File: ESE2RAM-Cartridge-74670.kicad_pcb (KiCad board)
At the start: 2 copper layers, 100 x 60.5 mm, 26 parts, among them IC1 SRAM, IC2 SRAM, J1 BUS_MSX, U1 74HC670, U2 74HC670, U3 74HC138, U4 74HC00, U5 74HC32

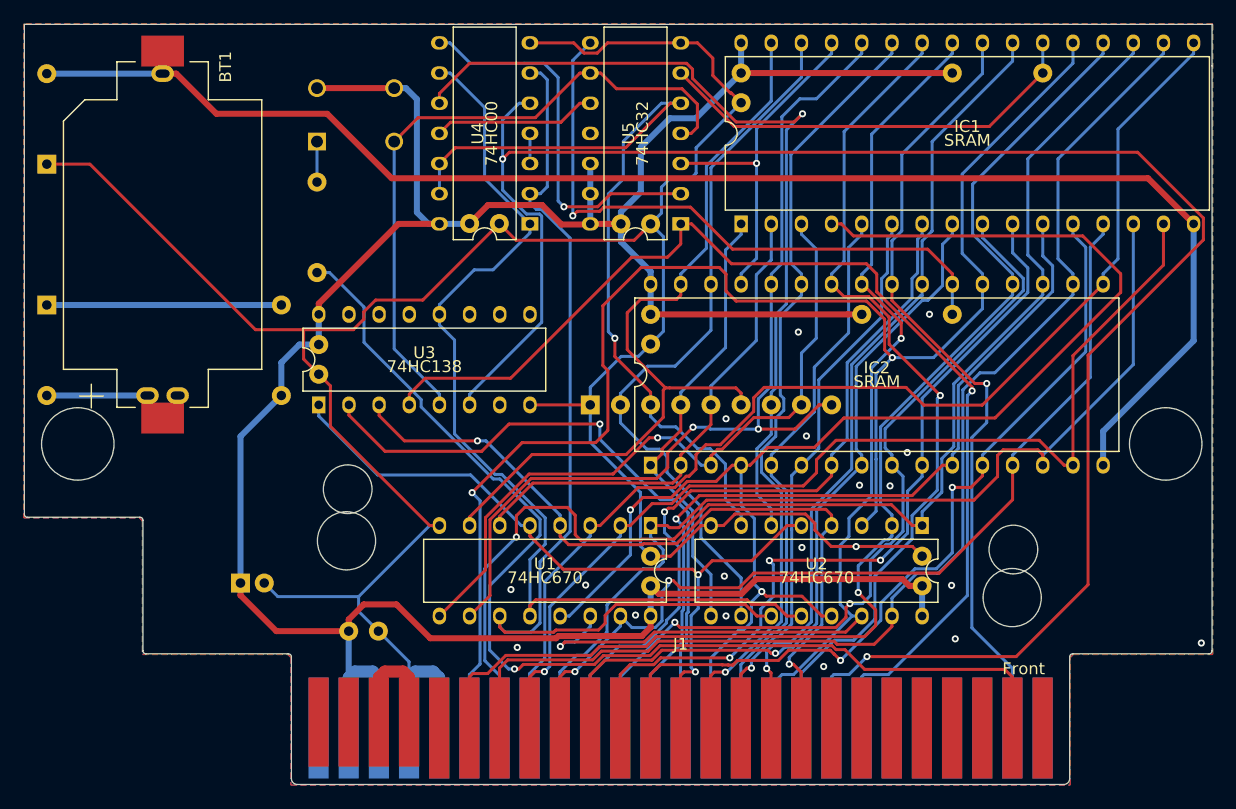
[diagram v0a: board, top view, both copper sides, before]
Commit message: Modify Schematic
プロジェクトローカルライブラリの設定が抜けていたのを修正。
Fixed missing project local library settings.
その他の細かな修正。
Other minor corrections.
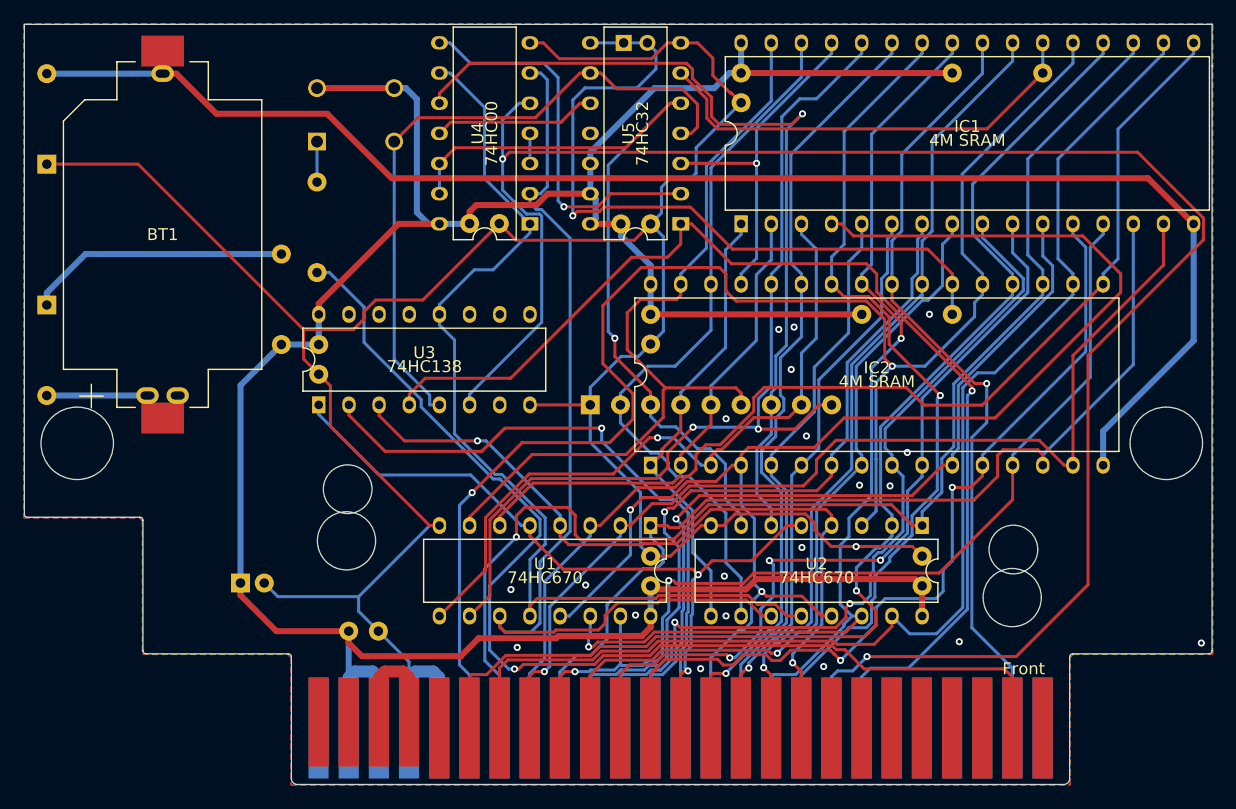
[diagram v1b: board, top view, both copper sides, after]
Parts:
- added J2: 8M, Connector_PinHeader_2.00mm:PinHeader_1x02_P2.00mm_Vertical, B.Cu at (90.2, 100.9)
- BT1: footprint _GoriponsoftLibrary:BatteryHolder_CH2x-2032LF -> ProjectLibrary:BatteryHolder_CH2x-2032LF
- IC1, IC2: value SRAM -> 4M SRAM; footprint _GoriponsoftLibrary:DIP32_600mil_FineLongPad -> ProjectLibrary:DIP32_600mil_FineLongPad
- S1: footprint SamacSys_Parts:DTS63NV -> ProjectLibrary:DTS63NV
- U1, U2, U3: footprint _GoriponsoftLibrary:DIP16_300mil_FineLongPad -> ProjectLibrary:DIP16_300mil_FineLongPad
- U4, U5: footprint _GoriponsoftLibrary:DIP14_300mil_FineLongPad -> ProjectLibrary:DIP14_300mil_FineLongPad
- moved R4 4.29 mm to (61.4, 126.3)
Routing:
- net /~{RAM1_CE}: track 53.2 -> 63.1 mm
- net /D0: track 78.4 -> 82.7 mm
- net /D4: track 101.2 -> 104.6 mm
- net /A11: track 99.6 -> 96.3 mm
- net /D7: track 127.4 -> 130.3 mm
- net Net-(D2-K): track 19.8 -> 22.1 mm
- net /A0: track 69.5 -> 71.7 mm
- net /A3: track 68.6 -> 70.2 mm
- net /A5: track 62.7 -> 64.3 mm
- net +5V: track 237.2 -> 235.7 mm
- net /EN_WR: track 72.0 -> 73.1 mm
- net /~{RAM0_CE}: track 36.7 -> 37.9 mm
- net /~{WR}: track 95.6 -> 96.2 mm
- net /A13: track 63.7 -> 63.2 mm
- net /A12: track 119.9 -> 120.5 mm
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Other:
- board text added: "似非²RAM rev.3 Goripon Hardware"
- board text removed: "似非²RAM rev.2 Goripon Hardware"

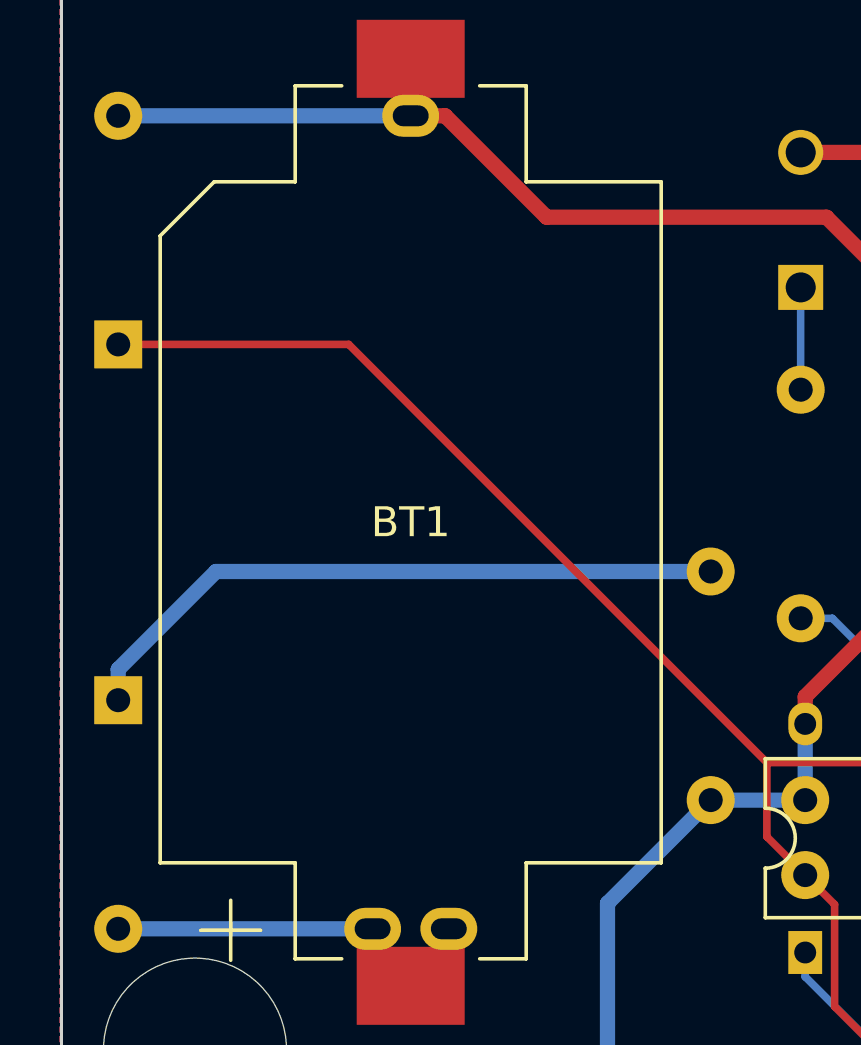
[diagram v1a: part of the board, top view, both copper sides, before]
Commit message: Modified Schematic
電解コンデンサの容量を10μFから47μFに変更
電池ソケットのシルク印刷の切り欠き位置が間違っていたのを修正
不要なファイルの削除
その他細かな修正
Changed the capacitance of electrolytic capacitor from 10uF to 47uF.
Fixed an issue where the notch position on the silkscreen print on the battery socket was incorrect.
Delete unnecessary files.
Other minor corrections.
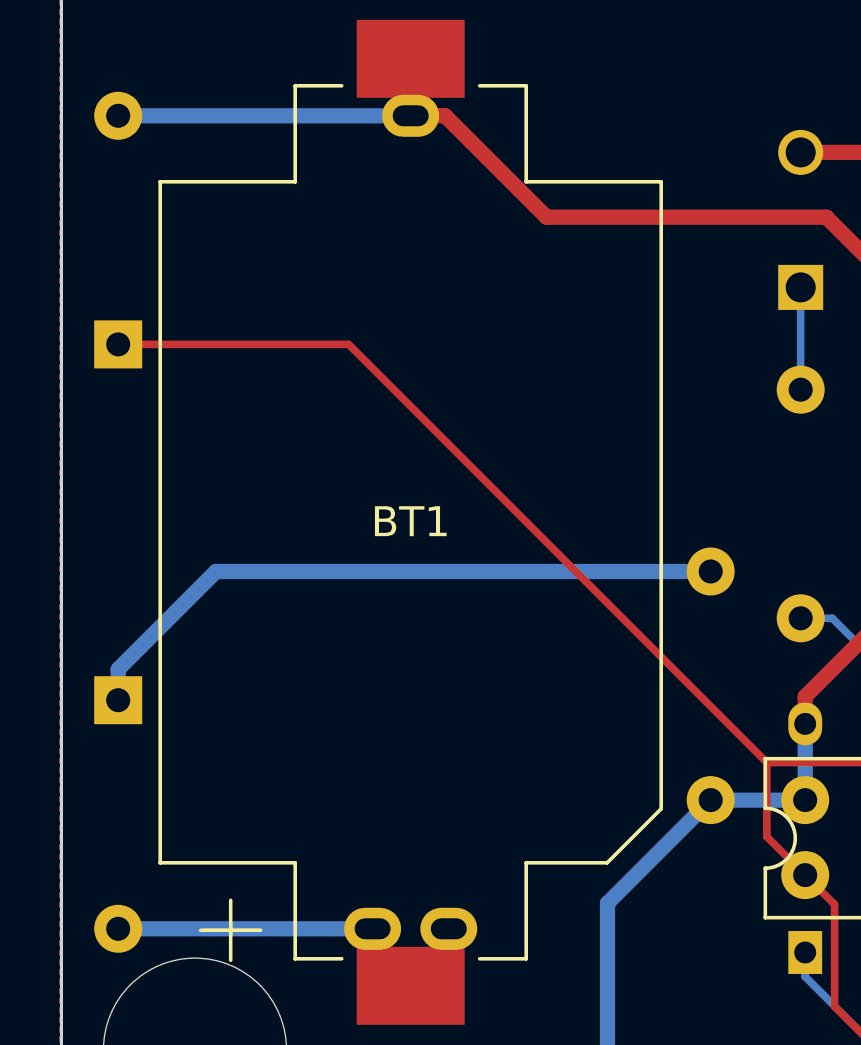
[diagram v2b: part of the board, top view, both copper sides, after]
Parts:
- C9: value 10u -> 47u
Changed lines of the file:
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@@
       (net 22 "/D6") (pinfunction "D6") (pintype "passive"))
     (pad "41" connect rect (at -20.32 -0.44) (size 1.7 8.5) (layers "B.Cu" "B.Mask")
-      (net 2 "GND") (pinfunction "GND") (pintype "passive"))
+      (net 2 "GND") (pinfunction "GND") (pintype "passive") (zone_connect 2))
     (pad "42" connect rect (at -20.32 -0.44) (size 1.7 8.5) (layers "F.Cu" "F.Mask")
       (net 51 "unconnected-(J1-CLOCK-Pad42)") (pinfunction "CLOCK") (pintype "passive+no_connect"))
     (pad "43" connect rect (at -22.86 -0.44) (size 1.7 8.5) (layers "B.Cu" "B.Mask")
-      (net 2 "GND") (pinfunction "GND") (pintype "passive"))
+      (net 2 "GND") (pinfunction "GND") (pintype "passive") (zone_connect 2))
     (pad "44" connect rect (at -22.86 -0.94) (size 1.7 7.5) (layers "F.Cu" "F.Mask")
       (net 52 "Net-(J1-SW1)") (pinfunction "SW1") (pintype "passive"))
@@
     (fp_line (start -11.35 -8.35) (end -11.35 -3.85)
       (stroke (width 0.12) (type solid)) (layer "F.SilkS"))
-    (fp_line (start -11.35 -8.35) (end 11.35 -8.35)
+    (fp_line (start -11.35 -8.35) (end 9.55 -8.35)
       (stroke (width 0.12) (type solid)) (layer "F.SilkS"))
     (fp_line (start -11.35 -3.85) (end -14.55 -3.85)
@@
     (fp_line (start -11.35 3.85) (end -14.55 3.85)
       (stroke (width 0.12) (type solid)) (layer "F.SilkS"))
-    (fp_line (start -11.35 6.55) (end -11.35 3.85)
-      (stroke (width 0.12) (type solid)) (layer "F.SilkS"))
-    (fp_line (start -9.55 8.35) (end -11.35 6.55)
-      (stroke (width 0.12) (type solid)) (layer "F.SilkS"))
-    (fp_line (start 11.35 -8.35) (end 11.35 -3.85)
+    (fp_line (start -11.35 8.35) (end -11.35 3.85)
+      (stroke (width 0.12) (type solid)) (layer "F.SilkS"))
+    (fp_line (start 9.55 -8.35) (end 11.35 -6.55)
+      (stroke (width 0.12) (type solid)) (layer "F.SilkS"))
+    (fp_line (start 11.35 -6.55) (end 11.35 -3.85)
       (stroke (width 0.12) (type solid)) (layer "F.SilkS"))
     (fp_line (start 11.35 -3.85) (end 14.55 -3.85)
@@
     (fp_line (start 11.35 3.85) (end 14.55 3.85)
       (stroke (width 0.12) (type solid)) (layer "F.SilkS"))
-    (fp_line (start 11.35 8.35) (end -9.55 8.35)
+    (fp_line (start 11.35 8.35) (end -11.35 8.35)
       (stroke (width 0.12) (type solid)) (layer "F.SilkS"))
     (fp_line (start 11.35 8.35) (end 11.35 3.85)
@@
     (fp_circle (center 0 0) (end -10.2 0)
       (stroke (width 0.3) (type solid)) (fill none) (layer "Dwgs.User"))
-    (fp_line (start -17.2 2.3) (end -17.2 -2.3)
-      (stroke (width 0.05) (type solid)) (layer "F.CrtYd"))
-    (fp_line (start -17.2 2.3) (end -14.7 2.3)
-      (stroke (width 0.05) (type default)) (layer "F.CrtYd"))
+    (fp_line (start -17.2 -2.3) (end -17.2 2.3)
+      (stroke (width 0.05) (type solid)) (layer "F.CrtYd"))
+    (fp_line (start -14.7 -4) (end -14.7 -2.3)
+      (stroke (width 0.05) (type solid)) (layer "F.CrtYd"))
     (fp_line (start -14.7 -4) (end -11.5 -4)
       (stroke (width 0.05) (type solid)) (layer "F.CrtYd"))
     (fp_line (start -14.7 -2.3) (end -17.2 -2.3)
       (stroke (width 0.05) (type default)) (layer "F.CrtYd"))
-    (fp_line (start -14.7 -2.3) (end -14.7 -4)
-      (stroke (width 0.05) (type solid)) (layer "F.CrtYd"))
-    (fp_line (start -14.7 4) (end -14.7 2.3)
-      (stroke (width 0.05) (type solid)) (layer "F.CrtYd"))
-    (fp_line (start -14.7 4) (end -11.5 4)
+    (fp_line (start -14.7 2.3) (end -17.2 2.3)
+      (stroke (width 0.05) (type default)) (layer "F.CrtYd"))
+    (fp_line (start -14.7 2.3) (end -14.7 4)
       (stroke (width 0.05) (type solid)) (layer "F.CrtYd"))
     (fp_line (start -11.5 -8.5) (end -6.5 -8.5)
@@
     (fp_line (start -11.5 -4) (end -11.5 -8.5)
       (stroke (width 0.05) (type solid)) (layer "F.CrtYd"))
-    (fp_line (start -11.5 4) (end -11.5 8.5)
-      (stroke (width 0.05) (type solid)) (layer "F.CrtYd"))
-    (fp_line (start -6.5 8.5) (end -11.5 8.5)
-      (stroke (width 0.05) (type solid)) (layer "F.CrtYd"))
-    (fp_line (start 11.5 -8.5) (end 6.5 -8.5)
-      (stroke (width 0.05) (type solid)) (layer "F.CrtYd"))
-    (fp_line (start 11.5 -8.5) (end 11.5 -4)
-      (stroke (width 0.05) (type solid)) (layer "F.CrtYd"))
-    (fp_line (start 11.5 -4) (end 14.7 -4)
+    (fp_line (start -11.5 4) (end -14.7 4)
+      (stroke (width 0.05) (type solid)) (layer "F.CrtYd"))
+    (fp_line (start -11.5 8.5) (end -11.5 4)
+      (stroke (width 0.05) (type solid)) (layer "F.CrtYd"))
+    (fp_line (start -11.5 8.5) (end -6.5 8.5)
+      (stroke (width 0.05) (type solid)) (layer "F.CrtYd"))
+    (fp_line (start 6.5 -8.5) (end 11.5 -8.5)
+      (stroke (width 0.05) (type solid)) (layer "F.CrtYd"))
+    (fp_line (start 11.5 -4) (end 11.5 -8.5)
       (stroke (width 0.05) (type solid)) (layer "F.CrtYd"))
     (fp_line (start 11.5 4) (end 11.5 8.5)
@@
     (fp_line (start 11.5 8.5) (end 6.5 8.5)
       (stroke (width 0.05) (type solid)) (layer "F.CrtYd"))
-    (fp_line (start 14.7 -2.3) (end 14.7 -4)
-      (stroke (width 0.05) (type solid)) (layer "F.CrtYd"))
-    (fp_line (start 14.7 -2.3) (end 17.2 -2.3)
-      (stroke (width 0.05) (type default)) (layer "F.CrtYd"))
+    (fp_line (start 14.7 -4) (end 11.5 -4)
+      (stroke (width 0.05) (type solid)) (layer "F.CrtYd"))
+    (fp_line (start 14.7 -4) (end 14.7 -2.3)
+      (stroke (width 0.05) (type solid)) (layer "F.CrtYd"))
+    (fp_line (start 14.7 2.3) (end 14.7 4)
+      (stroke (width 0.05) (type solid)) (layer "F.CrtYd"))
     (fp_line (start 14.7 2.3) (end 17.2 2.3)
       (stroke (width 0.05) (type default)) (layer "F.CrtYd"))
     (fp_line (start 14.7 4) (end 11.5 4)
       (stroke (width 0.05) (type solid)) (layer "F.CrtYd"))
-    (fp_line (start 14.7 4) (end 14.7 2.3)
-      (stroke (width 0.05) (type solid)) (layer "F.CrtYd"))
-    (fp_line (start 17.2 2.3) (end 17.2 -2.3)
+    (fp_line (start 17.2 -2.3) (end 14.7 -2.3)
+      (stroke (width 0.05) (type default)) (layer "F.CrtYd"))
+    (fp_line (start 17.2 -2.3) (end 17.2 2.3)
       (stroke (width 0.05) (type solid)) (layer "F.CrtYd"))
     (fp_arc (start -6.499999 -8.5) (mid 0 -10.700467) (end 6.5 -8.5)
       (stroke (width 0.05) (type solid)) (layer "F.CrtYd"))
-    (fp_arc (start 6.499999 8.5) (mid 0 10.700467) (end -6.5 8.5)
-      (stroke (width 0.05) (type solid)) (layer "F.CrtYd"))
-    (fp_line (start -14.2 -3.5) (end -11 -3.5)
-      (stroke (width 0.1) (type solid)) (layer "F.Fab"))
-    (fp_line (start -14.2 3.5) (end -14.2 -3.5)
+    (fp_arc (start 6.5 8.5) (mid 0 10.700467) (end -6.499999 8.5)
+      (stroke (width 0.05) (type solid)) (layer "F.CrtYd"))
+    (fp_line (start -14.2 3.5) (end -11 3.5)
       (stroke (width 0.1) (type solid)) (layer "F.Fab"))
     (fp_line (start -11 -8) (end -11 -3.5)
       (stroke (width 0.1) (type solid)) (layer "F.Fab"))
-    (fp_line (start -11 3.5) (end -14.2 3.5)
-      (stroke (width 0.1) (type solid)) (layer "F.Fab"))
-    (fp_line (start -11 6.4) (end -11 3.5)
-      (stroke (width 0.1) (type solid)) (layer "F.Fab"))
-    (fp_line (start -9.4 8) (end -11 6.4)
-      (stroke (width 0.1) (type solid)) (layer "F.Fab"))
-    (fp_line (start 11 -8) (end -11 -8)
-      (stroke (width 0.1) (type solid)) (layer "F.Fab"))
-    (fp_line (start 11 -8) (end 11 -3.5)
-      (stroke (width 0.1) (type solid)) (layer "F.Fab"))
-    (fp_line (start 11 3.5) (end 14.2 3.5)
-      (stroke (width 0.1) (type solid)) (layer "F.Fab"))
-    (fp_line (start 11 8) (end -9.4 8)
+    (fp_line (start -11 -8) (end 9.4 -8)
+      (stroke (width 0.1) (type solid)) (layer "F.Fab"))
+    (fp_line (start -11 -3.5) (end -14.2 -3.5)
+      (stroke (width 0.1) (type solid)) (layer "F.Fab"))
+    (fp_line (start -11 8) (end -11 3.5)
+      (stroke (width 0.1) (type solid)) (layer "F.Fab"))
+    (fp_line (start -11 8) (end 11 8)
+      (stroke (width 0.1) (type solid)) (layer "F.Fab"))
+    (fp_line (start 9.4 -8) (end 11 -6.4)
+      (stroke (width 0.1) (type solid)) (layer "F.Fab"))
+    (fp_line (start 11 -6.4) (end 11 -3.5)
+      (stroke (width 0.1) (type solid)) (layer "F.Fab"))
+    (fp_line (start 11 -3.5) (end 14.2 -3.5)
       (stroke (width 0.1) (type solid)) (layer "F.Fab"))
     (fp_line (start 11 8) (end 11 3.5)
       (stroke (width 0.1) (type solid)) (layer "F.Fab"))
-    (fp_line (start 14.2 -3.5) (end 11 -3.5)
-      (stroke (width 0.1) (type solid)) (layer "F.Fab"))
-    (fp_line (start 14.2 3.5) (end 14.2 -3.5)
+    (fp_line (start 14.2 -3.5) (end 14.2 3.5)
+      (stroke (width 0.1) (type solid)) (layer "F.Fab"))
+    (fp_line (start 14.2 -3.5) (end 14.2 3.5)
+      (stroke (width 0.1) (type solid)) (layer "F.Fab"))
+    (fp_line (start 14.2 3.5) (end 11 3.5)
       (stroke (width 0.1) (type solid)) (layer "F.Fab"))
     (pad "1" thru_hole oval (at 13.55 -1.27 90) (size 1.4 1.9) (drill oval 0.7 1.2) (layers "*.Cu" "*.Mask")
@@
         (effects (font (size 1 1) (thickness 0.153)) (justify mirror))
     )
-    (fp_text value "10u" (at 1 -3.75) (layer "B.SilkS")
-        (effects (font (size 1 1) (thickness 0.153)) (justify mirror))
-    )
+    (fp_text value "47u" (at 1 -3.75) (layer "B.SilkS")
+        (effects (font (size 1 1) (thickness 0.153)) (justify mirror))
+    )
